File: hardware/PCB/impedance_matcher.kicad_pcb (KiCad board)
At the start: 4 copper layers, 72 x 63 mm, 51 parts, among them Q1 PC817, U1 TLV2372IP

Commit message: Make more compact
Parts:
- FAN1, OLED1: footprint Project Connectors:B4B-XH-A -> Connector_JST:JST_PH_B4B-PH-K_1x04_P2.00mm_Vertical
- I2C1: footprint Project Connectors:B2B-XH-A -> Connector_JST:JST_PH_B2B-PH-K_1x02_P2.00mm_Vertical
- ROTARY1: footprint B5B-XH-A:JST_B5B-XH-A -> Connector_JST:JST_PH_B5B-PH-K_1x05_P2.00mm_Vertical
- SWR1: footprint Project Connectors:B3B-XH-A -> Connector_JST:JST_PH_B3B-PH-K_1x03_P2.00mm_Vertical
- moved ROTARY1 4.77 mm to (49.0, 31.4)
- moved I2C1 3.07 mm to (80.5, 31.4), turned to 0 degrees
- moved POWER1 1.81 mm to (36.8, 26.5), turned to 180 degrees
- moved FAN1 0.92 mm to (91.2, 31.4)
- moved FB1 0.91 mm to (39.6, 28.5)
- moved A1 0.77 mm to (100.4, 25.0)
- moved CR1 0.77 mm to (42.7, 35.5)
- moved R2 0.77 mm to (71.3, 36.6)
- moved R3 0.77 mm to (91.2, 36.5)
- moved R5 0.77 mm to (76.7, 36.6)
- moved R9 0.77 mm to (42.6, 31.7)
- moved OLED1 0.55 mm to (66.0, 31.4)
- moved SWR1 0.50 mm to (93.5, 70.5)
- moved REV_POLARITY1 0.23 mm to (36.2, 36.8)
- turned C3 to 180 degrees
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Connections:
- C3 pad 1: GND -> 5V
- C3 pad 2: 5V -> GND
- C4 pad 1: GND -> 5V
- C4 pad 2: 5V -> GND
- I2C1 pad 1: /SDA -> /SCL
- I2C1 pad 2: /SCL -> /SDA
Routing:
- net /DT: track 10.7 -> 7.34 mm
- net 5V: track 36.6 -> 33.2 mm
- net /CLK: track 10.6 -> 7.42 mm
- net /SW: track 10.8 -> 13.8 mm
- net /SCL: track 26.7 -> 23.9 mm
- net /SDA: track 26.8 -> 25.2 mm
- net 3.3V: track 133.8 -> 135.3 mm
- net /VIN: track 4.51 -> 3.20 mm
- net /FAN_CTRL: track 6.45 -> 7.21 mm
- net /DIR1: track 36.3 -> 35.5 mm
- net /STEP1: track 35.9 -> 35.3 mm
- net /FAN: track 8.84 -> 8.29 mm
- net /NET_REVPOL: track 15.3 -> 14.8 mm
- net GND: vias 18 -> 13
- removed copper zone on B.Cu, net GND
- removed copper zone on F.Cu, net GND
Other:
- board size 72 x 63 mm -> 71 x 63 mm

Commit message: Revert "Fix traces and make more compact"
This reverts commit 96239e169e8d7fc6dc4d81f6383f1f882c301b51.
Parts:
- FAN1, OLED1: footprint Connector_JST:JST_PH_B4B-PH-K_1x04_P2.00mm_Vertical -> Project Connectors:B4B-XH-A
- I2C1: footprint Connector_JST:JST_PH_B2B-PH-K_1x02_P2.00mm_Vertical -> Project Connectors:B2B-XH-A
- ROTARY1: footprint Connector_JST:JST_PH_B5B-PH-K_1x05_P2.00mm_Vertical -> B5B-XH-A:JST_B5B-XH-A
- SWR1: footprint Connector_JST:JST_PH_B3B-PH-K_1x03_P2.00mm_Vertical -> Project Connectors:B3B-XH-A
- moved ROTARY1 4.77 mm to (53.8, 31.5)
- moved I2C1 3.07 mm to (83.5, 32.0), turned to 180 degrees
- moved POWER1 1.81 mm to (35.8, 28.0), turned to 90 degrees
- moved FAN1 0.92 mm to (90.5, 32.0)
- moved FB1 0.91 mm to (40.3, 29.0)
- moved A1 0.77 mm to (101.1, 25.0)
- moved CR1 0.77 mm to (43.5, 35.5)
- moved R2 0.77 mm to (72.1, 36.6)
- moved R3 0.77 mm to (92.0, 36.5)
- moved R5 0.77 mm to (77.4, 36.6)
- moved R9 0.77 mm to (43.4, 31.7)
- moved OLED1 0.55 mm to (66.0, 32.0)
- moved SWR1 0.50 mm to (93.5, 71.0)
- moved REV_POLARITY1 0.23 mm to (36.0, 36.8)
- turned C3 to 0 degrees
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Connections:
- C3 pad 1: 5V -> GND
- C3 pad 2: GND -> 5V
- C4 pad 1: 5V -> GND
- C4 pad 2: GND -> 5V
- I2C1 pad 1: /SCL -> /SDA
- I2C1 pad 2: /SDA -> /SCL
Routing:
- net /DT: track 7.34 -> 10.7 mm
- net 5V: track 33.2 -> 36.6 mm
- net /CLK: track 7.42 -> 10.6 mm
- net /SW: track 13.8 -> 10.8 mm
- net /SCL: track 23.9 -> 26.7 mm
- net /SDA: track 25.2 -> 26.8 mm
- net 3.3V: track 135.3 -> 133.8 mm
- net /VIN: track 3.20 -> 4.51 mm
- net /FAN_CTRL: track 7.21 -> 6.45 mm
- net /DIR1: track 35.5 -> 36.3 mm
- net /STEP1: track 35.3 -> 35.9 mm
- net /FAN: track 8.29 -> 8.84 mm
- net /NET_REVPOL: track 14.8 -> 15.3 mm
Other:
- board size 71 x 63 mm -> 72 x 63 mm

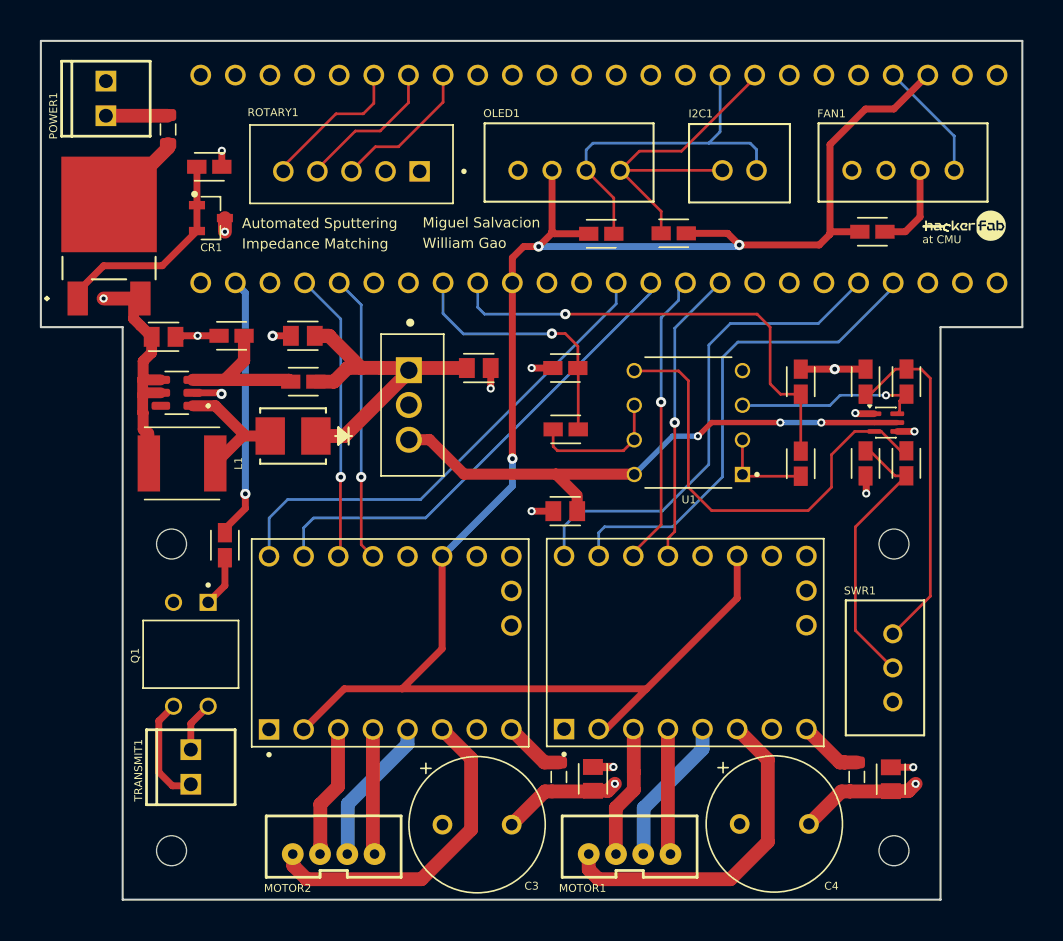
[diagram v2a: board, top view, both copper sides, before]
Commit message: Add stitching vias
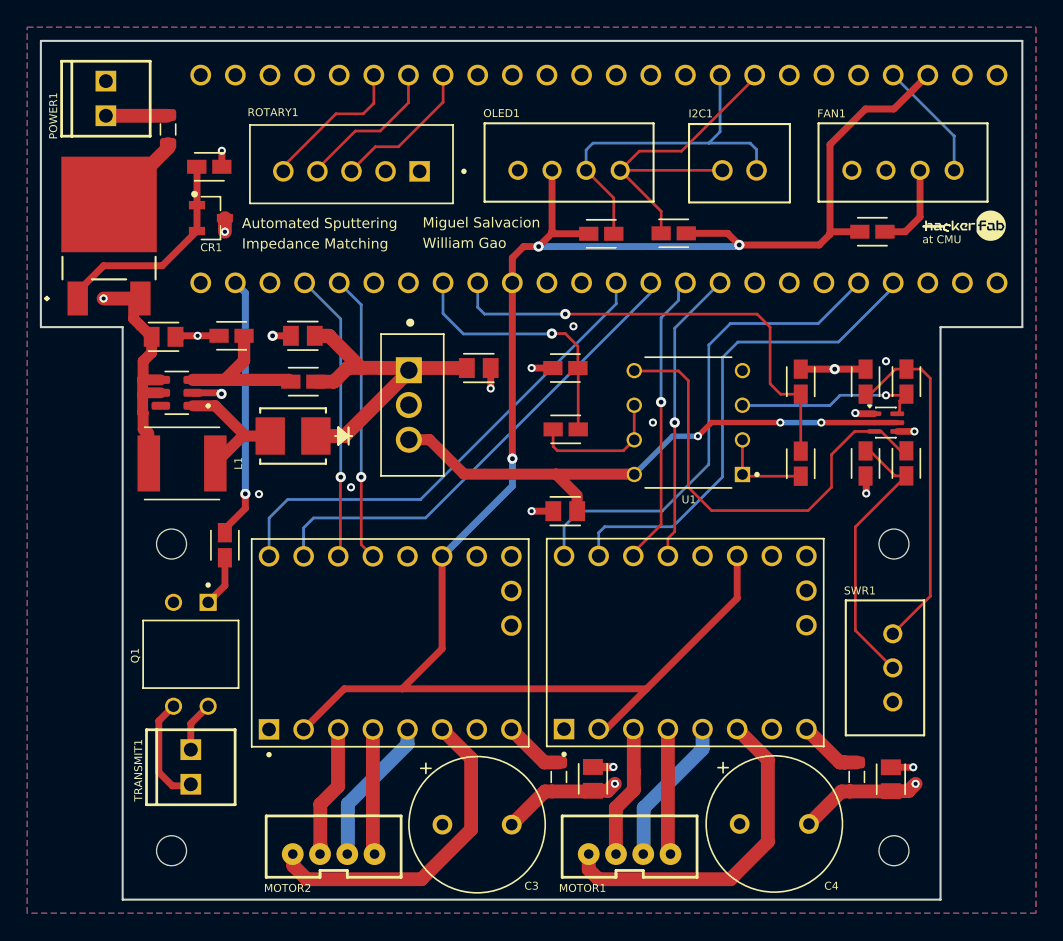
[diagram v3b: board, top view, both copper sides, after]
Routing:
- net GND: vias 13 -> 18
- added copper zone on B.Cu, net GND
- added copper zone on F.Cu, net GND
